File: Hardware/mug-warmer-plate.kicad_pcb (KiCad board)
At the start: 2 copper layers, 35 parts, among them J1 USB_C_Receptacle_USB2.0, J4 Conn_01x02_Male, Q1 IRLZ44N, SW1 SW_DIP_x01, U1 LM35-NEB, U2 ATtiny85-20P

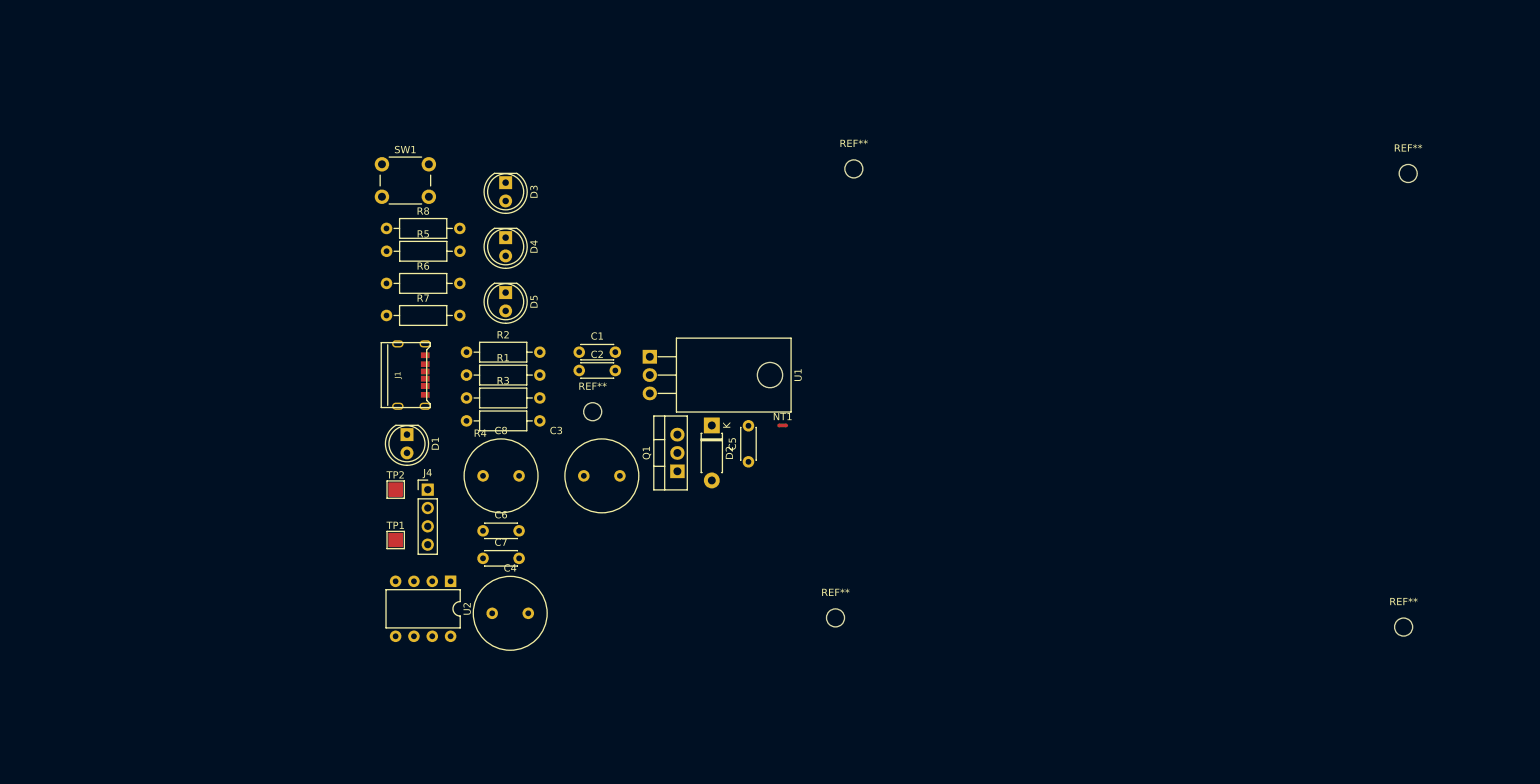
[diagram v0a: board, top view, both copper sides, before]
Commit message: Complete routing and pass DRC check
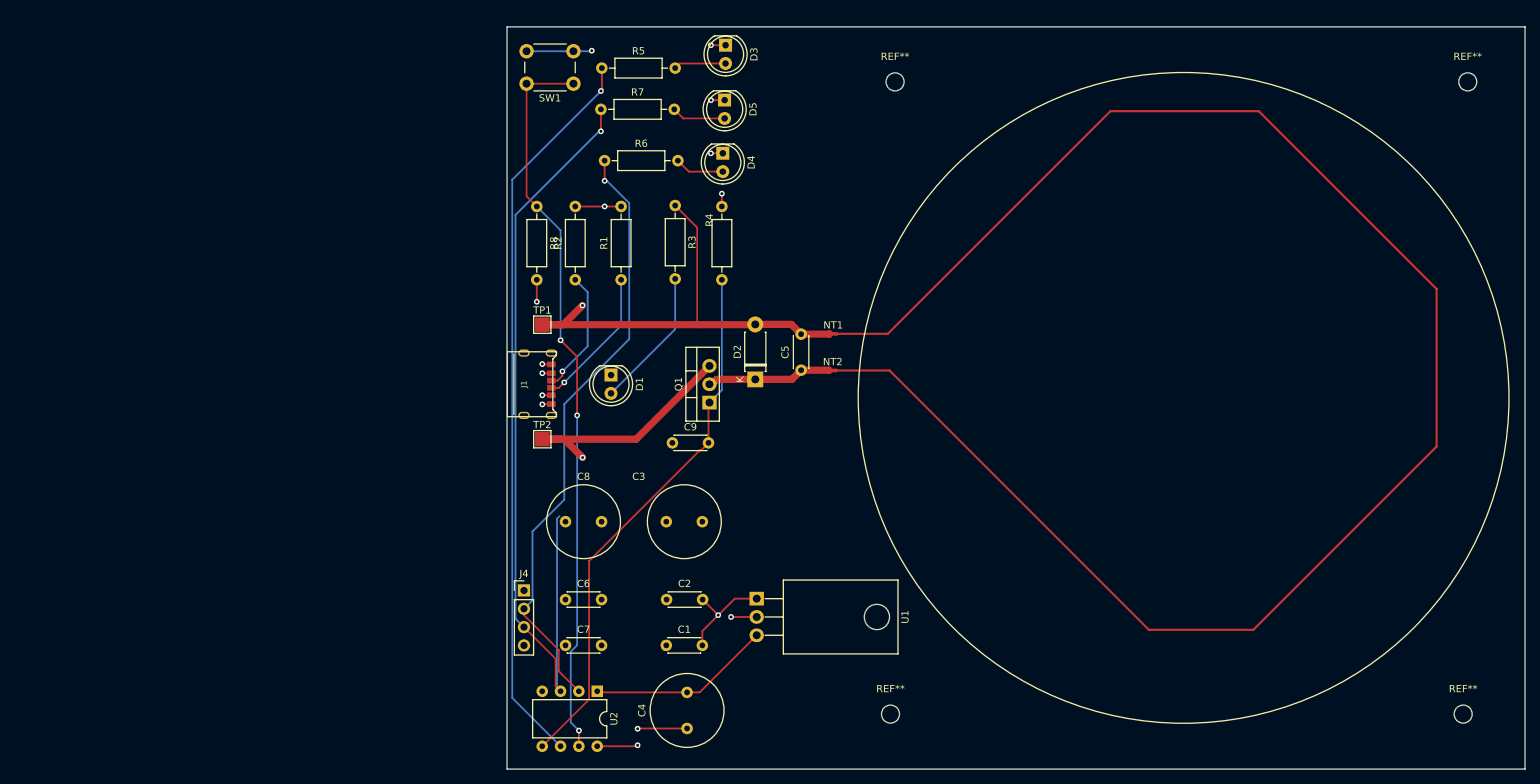
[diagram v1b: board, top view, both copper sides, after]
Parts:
- removed the REF** at (150.5, 104.1)
- added C9: 1uF, Capacitor_THT:C_Disc_D4.3mm_W1.9mm_P5.00mm, F.Cu at (161.5, 108.5)
- added NT2: NetTie_2, NetTie:NetTie-2_SMD_Pad0.5mm, F.Cu at (183.8, 98.4)
- moved C1 42.4 mm to (160.7, 136.5)
- moved R7 41.2 mm to (151.6, 62.2)
- moved D5 40.4 mm to (168.8, 61.0)
- moved R3 39.3 mm to (161.9, 75.6), turned to -90 degrees
- moved R5 39.2 mm to (151.8, 56.5)
- moved U1 36.7 mm to (173.2, 130.0)
- moved TP1 36.1 mm to (143.5, 92.1)
- moved D3 35.9 mm to (168.9, 53.3)
- moved R6 34.7 mm to (152.1, 69.3)
- moved C2 34.0 mm to (160.7, 130.2)
- moved D4 32.3 mm to (168.5, 68.3)
- moved R4 31.9 mm to (168.4, 85.9), turned to 90 degrees
- moved C4 31.4 mm to (163.6, 148.0), turned to 90 degrees
- moved D1 29.5 mm to (153.0, 99.1)
- moved SW1 28.8 mm to (147.8, 58.7), turned to 180 degrees
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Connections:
- C5 pad 1: ELEMENT -> Net-(C5-Pad1)
- D2 pad 1: ELEMENT -> Net-(C5-Pad1)
- Q1 pad 2: ELEMENT -> Net-(C5-Pad1)
- R6 pad 1: /RX -> /TX
- R7 pad 1: /TX -> /RX
- U2 pad 2: /RX -> /TX
- U2 pad 3: /TX -> /RX
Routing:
- net ELEMENT: track 0.00 -> 236.6 mm
- net /RX: track 0.00 -> 113.3 mm, vias 0 -> 1
- net Net-(R8-Pad1): track 0.00 -> 102.4 mm, vias 0 -> 3
- net Net-(R5-Pad1): track 0.00 -> 102.3 mm, vias 0 -> 1
- net +5V: track 0.00 -> 97.3 mm, vias 0 -> 6
- net /TX: track 0.00 -> 84.3 mm, vias 0 -> 1
- net GATE: track 0.00 -> 75.1 mm
- net GND: track 0.00 -> 63.8 mm, vias 0 -> 11
- net TEMP: track 0.00 -> 25.5 mm
- net Net-(R1-Pad1): track 0.00 -> 19.6 mm, vias 0 -> 1
- net Net-(D1-Pad2): track 0.00 -> 19.6 mm
- net Net-(C5-Pad1): track 0.00 -> 17.4 mm
- net Net-(R2-Pad1): track 0.00 -> 17.3 mm, vias 0 -> 1
- net Net-(D5-Pad2): track 0.00 -> 7.51 mm
- net Net-(D3-Pad2): track 0.00 -> 7.25 mm
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- added copper zone on In2.Cu, net +5V
- added copper zone on In1.Cu, net GND
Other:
- board outline added: 141.1 x 102.9 mm
- copper layers 2 -> 4

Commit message: Completed silkscreen layer
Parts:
- added TP3: 5V, TestPoint:TestPoint_Pad_2.0x2.0mm, F.Cu at (113.5, 88.6)
- added TP4: GND, TestPoint:TestPoint_Pad_2.0x2.0mm, F.Cu at (113.5, 99.8)
- TP1: value TestPoint -> 5V
- TP2: value TestPoint -> GND
- moved C2 68.2 mm to (92.5, 128.5)
- moved C9 68.2 mm to (93.3, 106.8)
- moved NT2 68.2 mm to (115.6, 96.8)
- moved Q1 68.2 mm to (98.5, 101.2)
- moved R3 68.2 mm to (93.7, 73.9)
- moved REF** 68.2 mm to (123.6, 144.4)
- moved U1 68.2 mm to (105.0, 128.4)
- moved C1 68.2 mm to (92.5, 134.9)
- moved C3 68.2 mm to (92.5, 117.7)
- moved C4 68.2 mm to (95.4, 146.4)
- moved C5 68.2 mm to (111.2, 96.7)
- moved C6 68.2 mm to (78.5, 128.5)
- moved C7 68.2 mm to (78.5, 134.9)
- moved C8 68.2 mm to (78.5, 117.7)
- moved D1 68.2 mm to (84.8, 97.4)
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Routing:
- net /RX: track 113.3 -> 88.7 mm
- net ELEMENT: track 236.6 -> 244.7 mm
- net Net-(C5-Pad1): track 17.4 -> 20.6 mm
- net +5V: track 97.3 -> 99.7 mm
- net Net-(D3-Pad2): track 7.25 -> 6.34 mm
- net Net-(R5-Pad1): track 102.3 -> 102.8 mm
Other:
- board text added: "0.1 Mug Warmer Plate"
- board text added: "5V"
- board text added: "GND"
- board text added: "Hot Zone Do Not Touch"
- board text added: "RX"
- board text added: "TX"

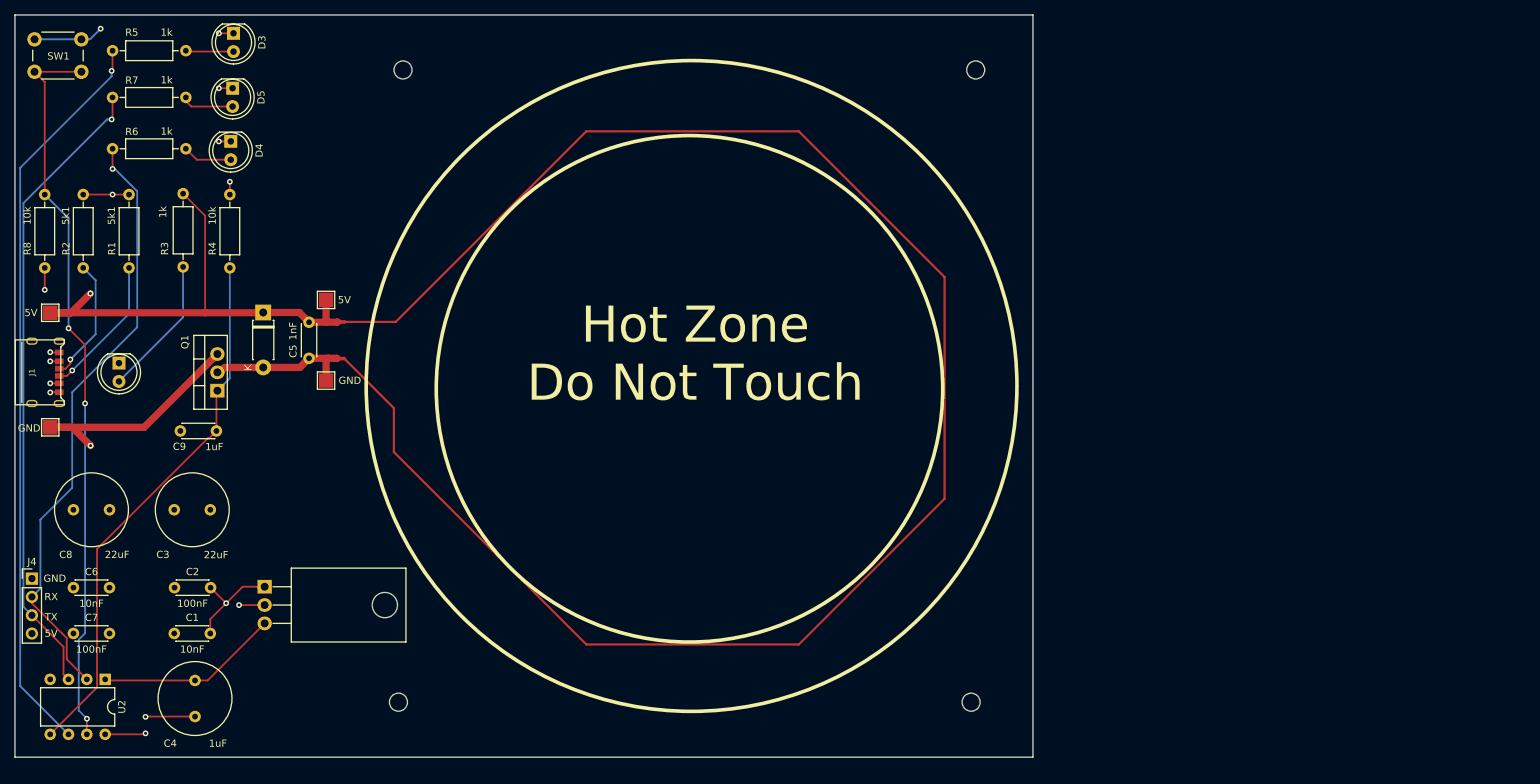
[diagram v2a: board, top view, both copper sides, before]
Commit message: Added cutout for thermal management
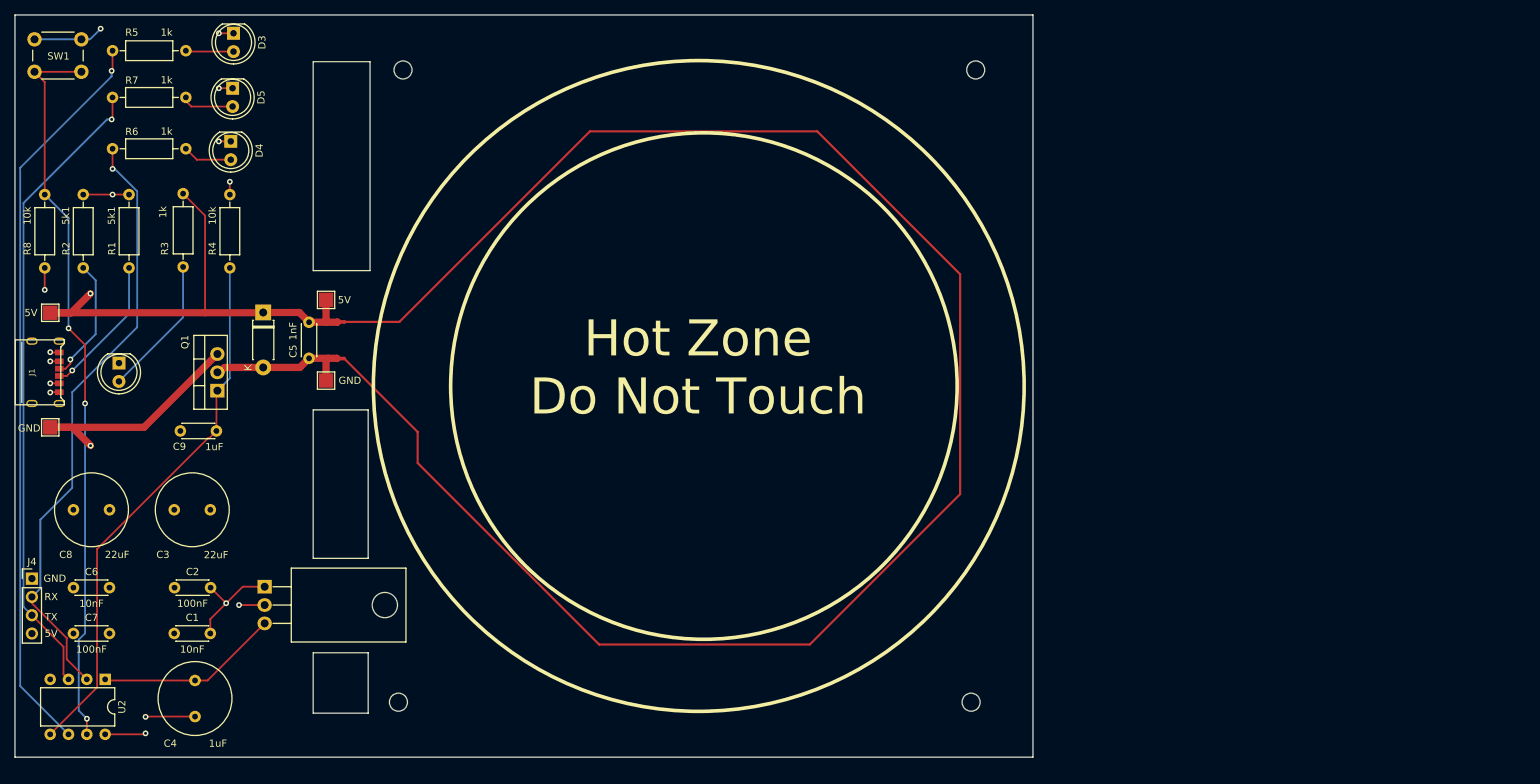
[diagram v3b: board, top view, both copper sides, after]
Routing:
- net ELEMENT: track 244.7 -> 247.8 mm
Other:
- outline, holes or cut-outs redrawn
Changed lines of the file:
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@@
       (outputformat 1)
       (mirror false)
-      (drillshape 1)
+      (drillshape 0)
       (scaleselection 1)
-      (outputdirectory "")
+      (outputdirectory "out/gerber/")
     )
   )
@@
   )
   (gr_circle (center 190.627 90.746278) (end 197.797722 90.746278) (layer "B.SilkS") (width 0.5) (fill none))
-  (gr_circle (center 164.197587 100.570587) (end 209.296 100.570587) (layer "F.SilkS") (width 0.5) (fill none))
-  (gr_circle (center 163.910587 100.965) (end 199.009 100.965) (layer "F.SilkS") (width 0.5) (fill none))
+  (gr_circle (center 165.197587 100.570587) (end 210.296 100.570587) (layer "F.SilkS") (width 0.5) (fill none))
+  (gr_circle (center 165.908413 100.584) (end 201.006826 100.584) (layer "F.SilkS") (width 0.5) (fill none))
+  (gr_rect (start 111.76 55.626) (end 119.634 84.582) (layer "Edge.Cuts") (width 0.1) (fill none))
+  (gr_rect (start 111.76 137.541) (end 119.38 145.923) (layer "Edge.Cuts") (width 0.1) (fill none))
   (gr_rect (start 211.5185 49.149) (end 70.4215 152.019) (layer "Edge.Cuts") (width 0.15) (fill none))
+  (gr_rect (start 111.76 103.886) (end 119.38 124.46) (layer "Edge.Cuts") (width 0.1) (fill none))
+  (gr_rect (start 119.38 124.46) (end 119.38 124.46) (layer "Edge.Cuts") (width 0.1) (fill none))
   (gr_text "0.1 \n\nMug Warmer Plate" (at 196.723 98.425) (layer "B.SilkS")
     (effects (font (size 5 5) (thickness 0.5)) (justify left mirror))
   )
-  (gr_text "Hot Zone\nDo Not Touch" (at 164.719 96.139) (layer "F.SilkS")
+  (gr_text "Hot Zone\nDo Not Touch" (at 165.1 98.044) (layer "F.SilkS")
     (effects (font (size 5 5) (thickness 0.5)))
   )
@@
   (via (at 88.519 146.431) (size 0.8) (drill 0.4) (layers "F.Cu" "B.Cu") (net 1))
   (via (at 83.947 74.041) (size 0.8) (drill 0.4) (layers "F.Cu" "B.Cu") (net 1))
-  (segment (start 149.606 136.398) (end 122.936 109.728) (width 0.3) (layer "F.Cu") (net 2))
-  (segment (start 116.126 91.694) (end 123.19 91.694) (width 0.3) (layer "F.Cu") (net 2))
-  (segment (start 122.936 109.728) (end 122.936 103.64) (width 0.3) (layer "F.Cu") (net 2))
-  (segment (start 123.19 91.694) (end 149.606 65.278) (width 0.3) (layer "F.Cu") (net 2))
-  (segment (start 149.606 65.278) (end 179.07 65.278) (width 0.3) (layer "F.Cu") (net 2))
-  (segment (start 199.263 116.205) (end 179.07 136.398) (width 0.3) (layer "F.Cu") (net 2))
-  (segment (start 199.263 85.471) (end 199.263 116.205) (width 0.3) (layer "F.Cu") (net 2))
-  (segment (start 122.936 103.64) (end 116.07 96.774) (width 0.3) (layer "F.Cu") (net 2))
-  (segment (start 179.07 136.398) (end 149.606 136.398) (width 0.3) (layer "F.Cu") (net 2))
-  (segment (start 179.07 65.278) (end 199.263 85.471) (width 0.3) (layer "F.Cu") (net 2))
+  (segment (start 151.384 136.398) (end 126.238 111.252) (width 0.3) (layer "F.Cu") (net 2))
+  (segment (start 180.594 136.398) (end 151.384 136.398) (width 0.3) (layer "F.Cu") (net 2))
+  (segment (start 201.422 115.57) (end 180.594 136.398) (width 0.3) (layer "F.Cu") (net 2))
+  (segment (start 126.238 106.942) (end 116.07 96.774) (width 0.3) (layer "F.Cu") (net 2))
+  (segment (start 123.698 91.694) (end 150.114 65.278) (width 0.3) (layer "F.Cu") (net 2))
+  (segment (start 181.61 65.278) (end 201.422 85.09) (width 0.3) (layer "F.Cu") (net 2))
+  (segment (start 116.126 91.694) (end 123.698 91.694) (width 0.3) (layer "F.Cu") (net 2))
+  (segment (start 126.238 111.252) (end 126.238 106.942) (width 0.3) (layer "F.Cu") (net 2))
+  (segment (start 150.114 65.278) (end 181.61 65.278) (width 0.3) (layer "F.Cu") (net 2))
+  (segment (start 201.422 85.09) (end 201.422 115.57) (width 0.3) (layer "F.Cu") (net 2))
   (segment (start 83.078 141.391) (end 82.921 141.234) (width 0.25) (layer "F.Cu") (net 3))
   (segment (start 95.377 141.391) (end 97.115 141.391) (width 0.25) (layer "F.Cu") (net 3))

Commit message: Added JLPCB order number id
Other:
- board text added: "JLCJLCJLCJLC"
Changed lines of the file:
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@@
   (gr_rect (start 111.76 103.886) (end 119.38 124.46) (layer "Edge.Cuts") (width 0.1) (fill none))
   (gr_rect (start 119.38 124.46) (end 119.38 124.46) (layer "Edge.Cuts") (width 0.1) (fill none))
+  (gr_text "JLCJLCJLCJLC" (at 205.486 150.368) (layer "B.Cu")
+    (effects (font (size 1 1) (thickness 0.15)) (justify mirror))
+  )
   (gr_text "0.1 \n\nMug Warmer Plate" (at 196.723 98.425) (layer "B.SilkS")
     (effects (font (size 5 5) (thickness 0.5)) (justify left mirror))
